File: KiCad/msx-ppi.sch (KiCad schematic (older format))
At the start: 13 parts, among them J1 Conn_02x13_Odd_Even, P1 CONN_02X25, Q1 BC547, SW1 SW_DIP_x08, U1 74LS138, U2 74LS32, U3 82C55A

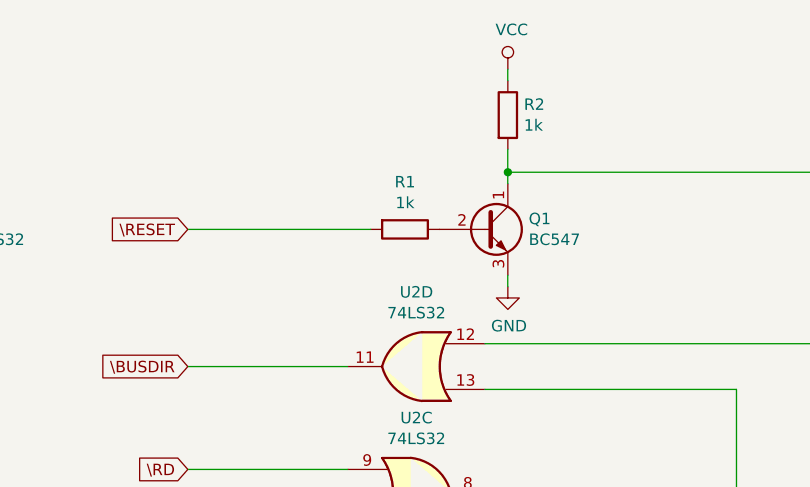
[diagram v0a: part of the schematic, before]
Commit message: Changed R2 value to 10k (was 1k)
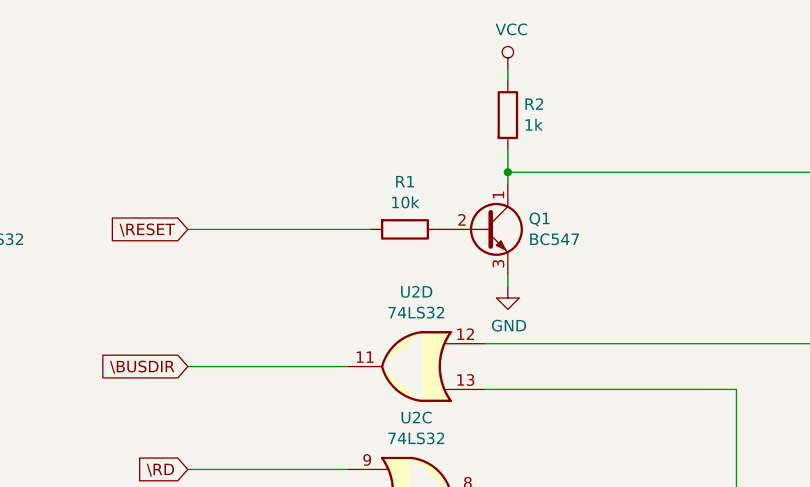
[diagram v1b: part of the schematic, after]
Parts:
- R1: value 1k -> 10k
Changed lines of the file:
@@
 P 4600 1800
 F 0 "R1" V 4393 1800 50  0000 C CNN
-F 1 "1k" V 4484 1800 50  0000 C CNN
+F 1 "10k" V 4484 1800 50  0000 C CNN
 F 2 "Resistor_THT:R_Axial_DIN0204_L3.6mm_D1.6mm_P7.62mm_Horizontal" V 4530 1800 50  0001 C CNN
 F 3 "~" H 4600 1800 50  0001 C CNN
